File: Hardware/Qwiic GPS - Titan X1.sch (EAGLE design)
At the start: 36 parts, among them J1 U.FL, J2 Qwiic Right Angle, J3 PTH, J4 Qwiic Right Angle, U1 Titan X1 GPS

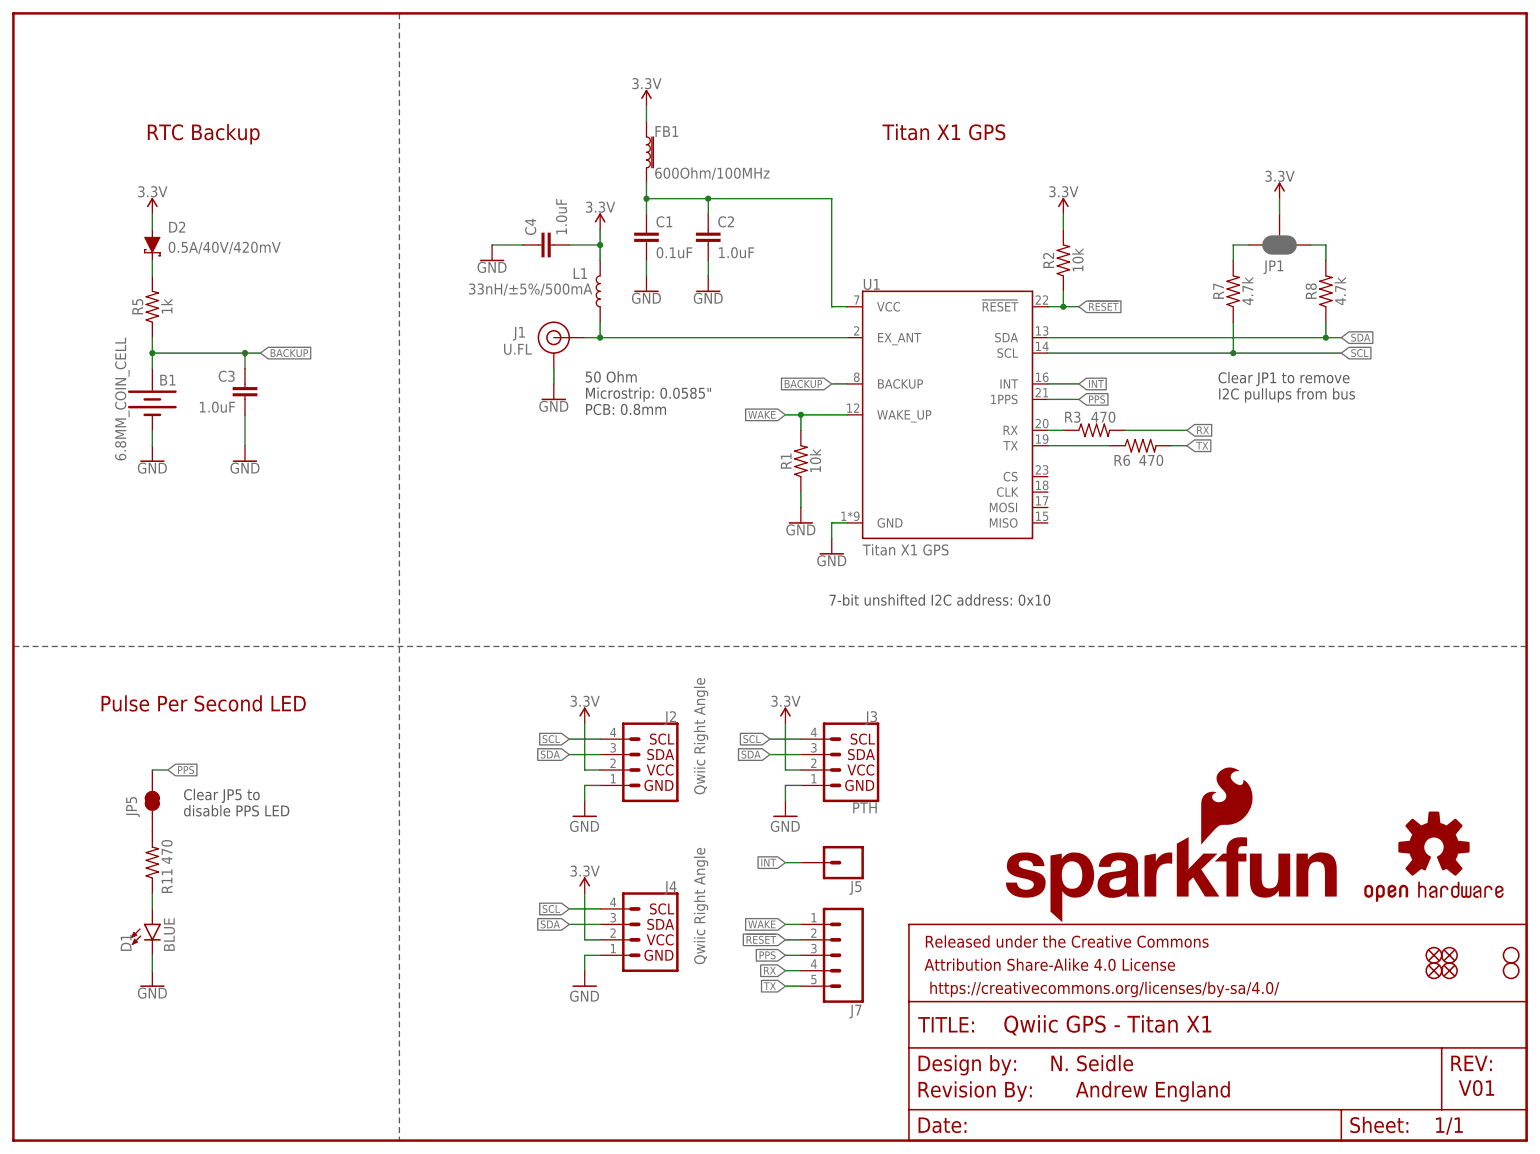
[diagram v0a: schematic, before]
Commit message: V02 changed some net issues, board thicknessinstruction
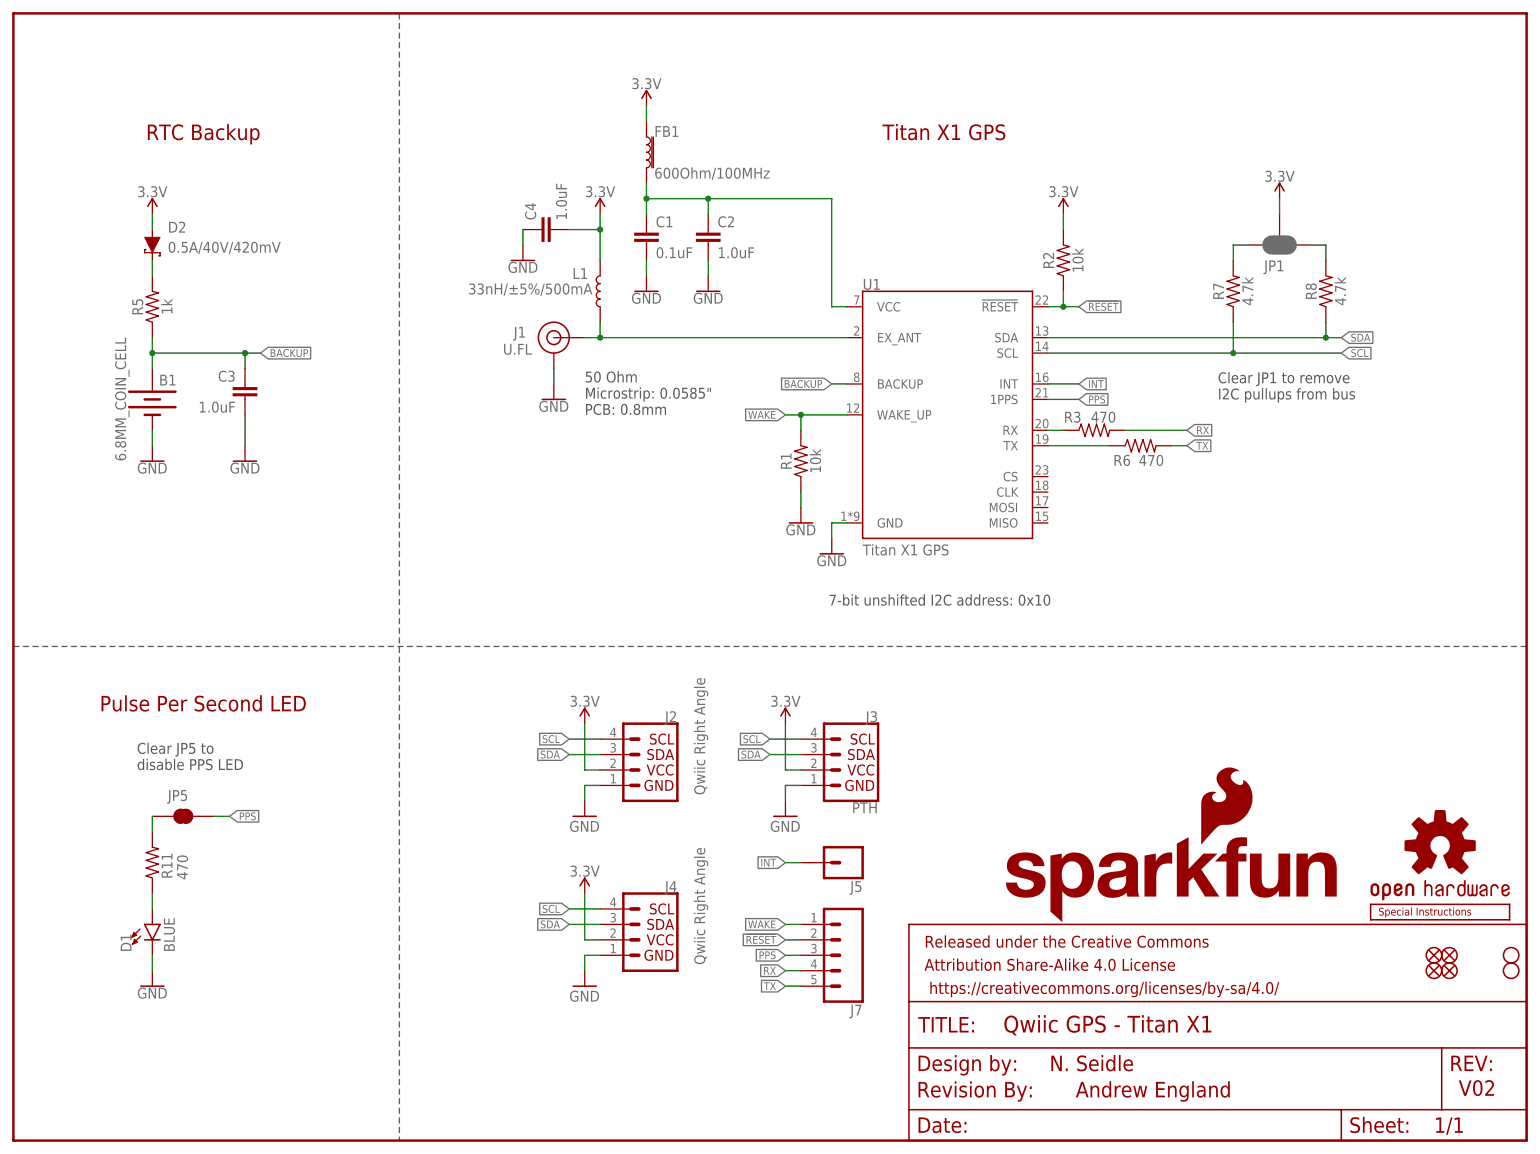
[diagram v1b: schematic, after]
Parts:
- added U$3: SPECIAL_INSTRUCTIONS-PRODUCTION, SparkFun-Aesthetics:SPECIAL_INSTRUCTIONS-PRODUCTION
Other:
- note added: "V02"
- note removed: "V01"
- moved on the sheet: C4, JP5
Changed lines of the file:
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@@
 <part name="JP7" library="SparkFun" deviceset="FIDUCIAL" device="UFIDUCIAL"/>
 <part name="JP8" library="SparkFun" deviceset="FIDUCIAL" device="UFIDUCIAL"/>
+<part name="U$3" library="SparkFun-Aesthetics" deviceset="SPECIAL_INSTRUCTIONS" device="-PRODUCTION"/>
 </parts>
 <sheets>
@@
 <plain>
 <text x="170.434" y="11.43" size="2.54" layer="94">N. Seidle</text>
-<text x="237.744" y="7.366" size="2.54" layer="94">V01</text>
+<text x="237.744" y="7.366" size="2.54" layer="94">V02</text>
 <text x="152.4" y="88.9" size="1.778" layer="97" align="center">7-bit unshifted I2C address: 0x10</text>
 <text x="153.162" y="165.862" size="2.54" layer="94" ratio="15" rot="MR180" align="center">Titan X1 GPS</text>
@@
 <text x="198.12" y="121.92" size="1.778" layer="97">Clear JP1 to remove
 I2C pullups from bus</text>
-<text x="27.94" y="53.34" size="1.778" layer="97">Clear JP5 to
+<text x="20.32" y="60.96" size="1.778" layer="97">Clear JP5 to
 disable PPS LED</text>
 </plain>
@@
 </instance>
 <instance part="GND8" gate="1" x="93.98" y="25.4"/>
-<instance part="LOGO1" gate="G$1" x="233.68" y="48.26"/>
+<instance part="LOGO1" gate="G$1" x="234.696" y="48.514"/>
 <instance part="J5" gate="G$1" x="137.16" y="45.72" rot="R180"/>
 <instance part="C2" gate="G$1" x="114.3" y="147.32"/>
@@
 <instance part="D1" gate="G$1" x="22.86" y="35.56"/>
 <instance part="GND12" gate="1" x="88.9" y="121.92"/>
-<instance part="JP5" gate="G$1" x="22.86" y="55.88" rot="R90"/>
+<instance part="JP5" gate="G$1" x="27.94" y="53.34"/>
 <instance part="L1" gate="G$1" x="96.52" y="139.7" smashed="yes" rot="R180">
 <attribute name="NAME" x="91.948" y="141.732" size="1.778" layer="95" font="vector"/>
 <attribute name="VALUE" x="95.25" y="139.192" size="1.778" layer="96" font="vector" rot="R180" align="top-left"/>
 </instance>
-<instance part="C4" gate="G$1" x="88.9" y="147.32" rot="R90"/>
-<instance part="GND13" gate="1" x="78.74" y="144.78"/>
-<instance part="SUPPLY3" gate="G$1" x="96.52" y="149.86" rot="MR0"/>
+<instance part="C4" gate="G$1" x="88.9" y="149.86" rot="R90"/>
+<instance part="GND13" gate="1" x="83.82" y="144.78"/>
+<instance part="SUPPLY3" gate="G$1" x="96.52" y="152.4" rot="MR0"/>
 <instance part="D2" gate="G$1" x="22.86" y="147.32" smashed="yes" rot="R270">
 <attribute name="NAME" x="25.4" y="149.352" size="1.778" layer="95" font="vector"/>
@@
 <instance part="J7" gate="G$1" x="137.16" y="30.48" rot="R180"/>
 <instance part="R11" gate="G$1" x="22.86" y="45.72" smashed="yes" rot="R90">
-<attribute name="NAME" x="26.162" y="42.672" size="1.778" layer="95" font="vector" rot="R90" align="bottom-center"/>
-<attribute name="VALUE" x="26.162" y="47.498" size="1.778" layer="96" font="vector" rot="R270" align="top-center"/>
+<attribute name="NAME" x="26.162" y="45.212" size="1.778" layer="95" font="vector" rot="R90" align="bottom-center"/>
+<attribute name="VALUE" x="28.702" y="44.958" size="1.778" layer="96" font="vector" rot="R270" align="top-center"/>
 </instance>
 <instance part="J1" gate="G$1" x="88.9" y="132.08" smashed="yes">
@@
 <instance part="JP7" gate="G$1" x="233.68" y="27.94" rot="R270"/>
 <instance part="JP8" gate="G$1" x="236.22" y="27.94" rot="R270"/>
+<instance part="U$3" gate="G$1" x="223.266" y="36.322"/>
 </instances>
 <busses>
@@
 <pinref part="SUPPLY3" gate="G$1" pin="3.3V"/>
 <pinref part="L1" gate="G$1" pin="2"/>
-<wire x1="96.52" y1="149.86" x2="96.52" y2="147.32" width="0.1524" layer="91"/>
+<wire x1="96.52" y1="152.4" x2="96.52" y2="149.86" width="0.1524" layer="91"/>
 <pinref part="C4" gate="G$1" pin="2"/>
-<wire x1="96.52" y1="147.32" x2="96.52" y2="144.78" width="0.1524" layer="91"/>
-<wire x1="91.44" y1="147.32" x2="96.52" y2="147.32" width="0.1524" layer="91"/>
-<junction x="96.52" y="147.32"/>
+<wire x1="96.52" y1="149.86" x2="96.52" y2="144.78" width="0.1524" layer="91"/>
+<wire x1="91.44" y1="149.86" x2="96.52" y2="149.86" width="0.1524" layer="91"/>
+<junction x="96.52" y="149.86"/>
 </segment>
 <segment>
@@
 <pinref part="C4" gate="G$1" pin="1"/>
 <pinref part="GND13" gate="1" pin="GND"/>
-<wire x1="78.74" y1="147.32" x2="83.82" y2="147.32" width="0.1524" layer="91"/>
+<wire x1="83.82" y1="149.86" x2="83.82" y2="147.32" width="0.1524" layer="91"/>
 </segment>
 <segment>
 <pinref part="D1" gate="G$1" pin="C"/>
+<pinref part="GND4" gate="1" pin="GND"/>
 <wire x1="22.86" y1="30.48" x2="22.86" y2="27.94" width="0.1524" layer="91"/>
-<pinref part="GND4" gate="1" pin="GND"/>
 </segment>
 <segment>
@@
 </segment>
 <segment>
-<wire x1="22.86" y1="60.96" x2="25.4" y2="60.96" width="0.1524" layer="91"/>
-<label x="25.4" y="60.96" size="1.27" layer="95" xref="yes"/>
+<wire x1="33.02" y1="53.34" x2="35.56" y2="53.34" width="0.1524" layer="91"/>
+<label x="35.56" y="53.34" size="1.27" layer="95" xref="yes"/>
 <pinref part="JP5" gate="G$1" pin="2"/>
 </segment>
@@
 <pinref part="JP5" gate="G$1" pin="1"/>
 <pinref part="R11" gate="G$1" pin="2"/>
-</segment>
-</net>
+<wire x1="22.86" y1="53.34" x2="22.86" y2="50.8" width="0.1524" layer="91"/>
+</segment>
+</net>

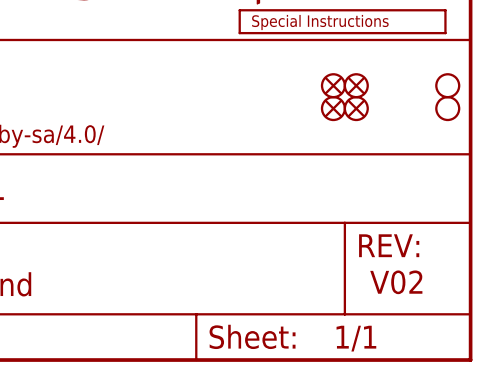
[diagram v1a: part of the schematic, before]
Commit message: Changed version number, moved int pin to be compatible with arduino, added jumper label for pps led
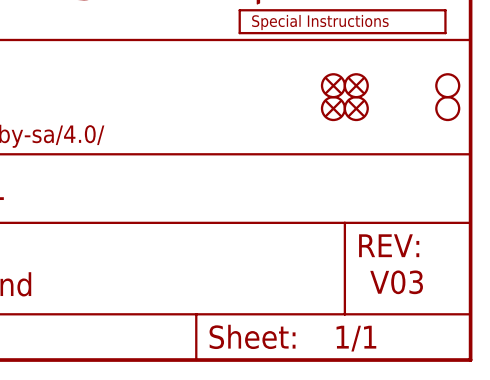
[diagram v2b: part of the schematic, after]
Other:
- note added: "V03"
- note removed: "V02"
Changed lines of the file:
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@@
 <plain>
 <text x="170.434" y="11.43" size="2.54" layer="94">N. Seidle</text>
-<text x="237.744" y="7.366" size="2.54" layer="94">V02</text>
+<text x="237.744" y="7.366" size="2.54" layer="94">V03</text>
 <text x="152.4" y="88.9" size="1.778" layer="97" align="center">7-bit unshifted I2C address: 0x10</text>
 <text x="153.162" y="165.862" size="2.54" layer="94" ratio="15" rot="MR180" align="center">Titan X1 GPS</text>

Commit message: updated version number
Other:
- note added: "V10"
- note removed: "V03"
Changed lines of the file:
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@@
 <plain>
 <text x="170.434" y="11.43" size="2.54" layer="94">N. Seidle</text>
-<text x="237.744" y="7.366" size="2.54" layer="94">V03</text>
+<text x="237.744" y="7.366" size="2.54" layer="94">V10</text>
 <text x="152.4" y="88.9" size="1.778" layer="97" align="center">7-bit unshifted I2C address: 0x10</text>
 <text x="153.162" y="165.862" size="2.54" layer="94" ratio="15" rot="MR180" align="center">Titan X1 GPS</text>
